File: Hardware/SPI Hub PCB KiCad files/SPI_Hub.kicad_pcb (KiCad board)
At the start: 4 copper layers, 90 x 65 mm, 22 parts, among them J1 Conn_01x08_Pin, J2 Left Front, J3 Left Center, J4 Left Rear, J5 Right Front, J6 Right Center, J7 Right Rear, U1 74AHC595, U2 74HC14

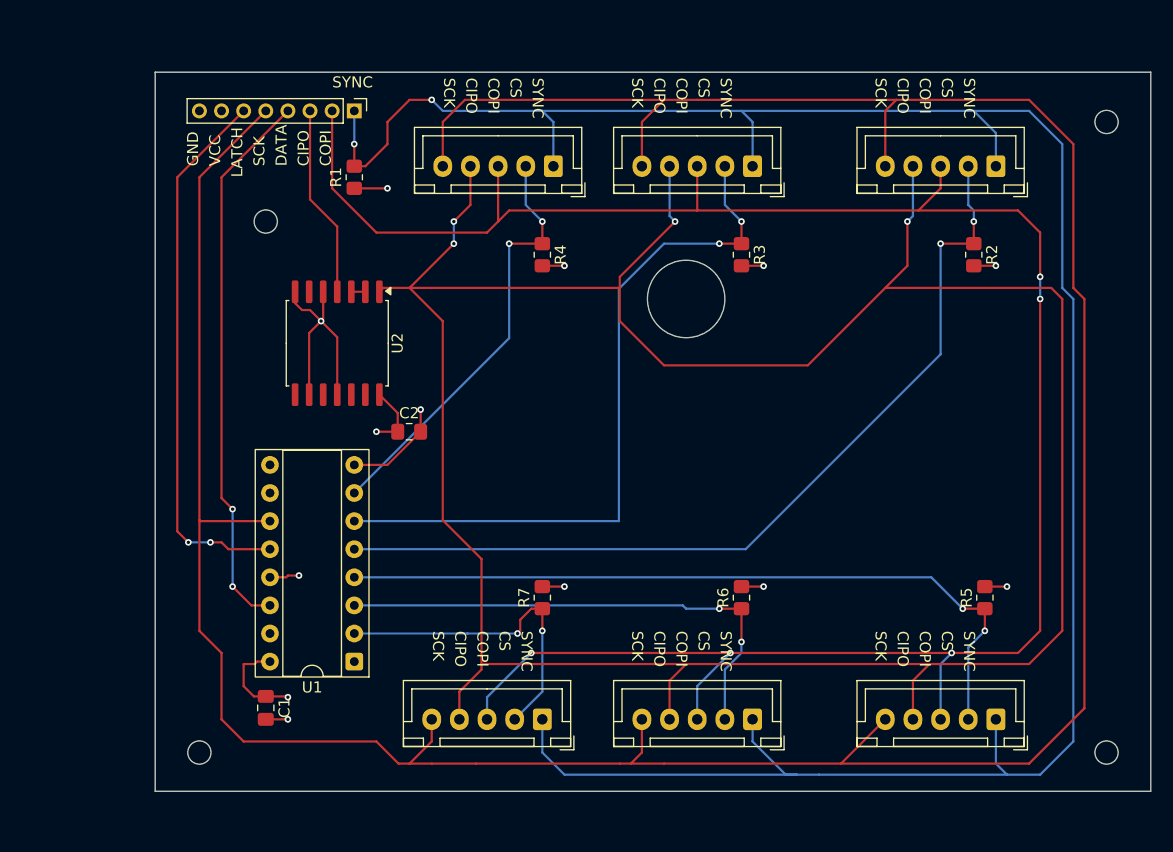
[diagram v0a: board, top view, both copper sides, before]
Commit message: Updated KiCad schematic, tied unused Schmitt input to gnd
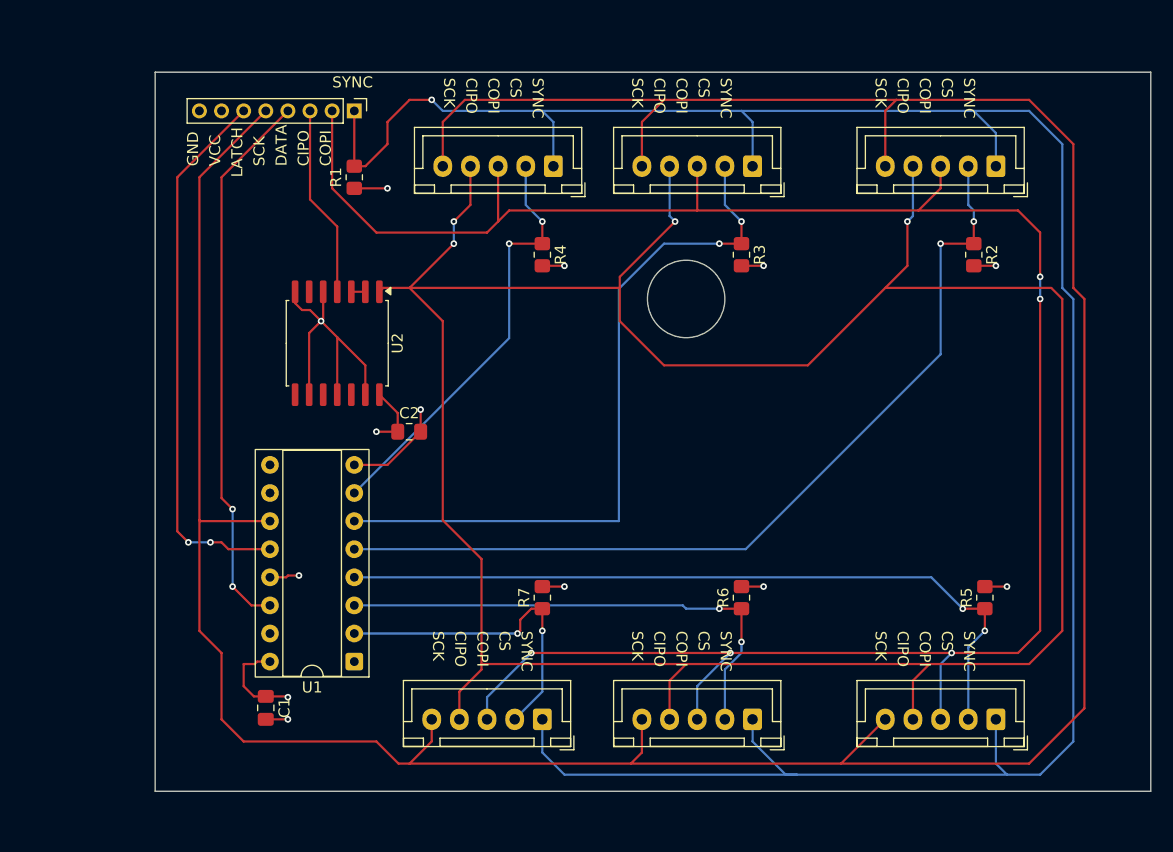
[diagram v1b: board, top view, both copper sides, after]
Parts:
- removed REF** (x4): MountingHole_2.1mm, MountingHole:MountingHole_2.1mm
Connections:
- net Net-(J2-Pin_4) renamed /cipo_peripheral
- U2 pad 13: unconnected-(U2-Pad13) -> GND
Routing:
- net GND: track 35.1 -> 41.3 mm
- net /trigger: track 211.8 -> 211.1 mm, vias 2 -> 1

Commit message: Updated and simplified PCB design
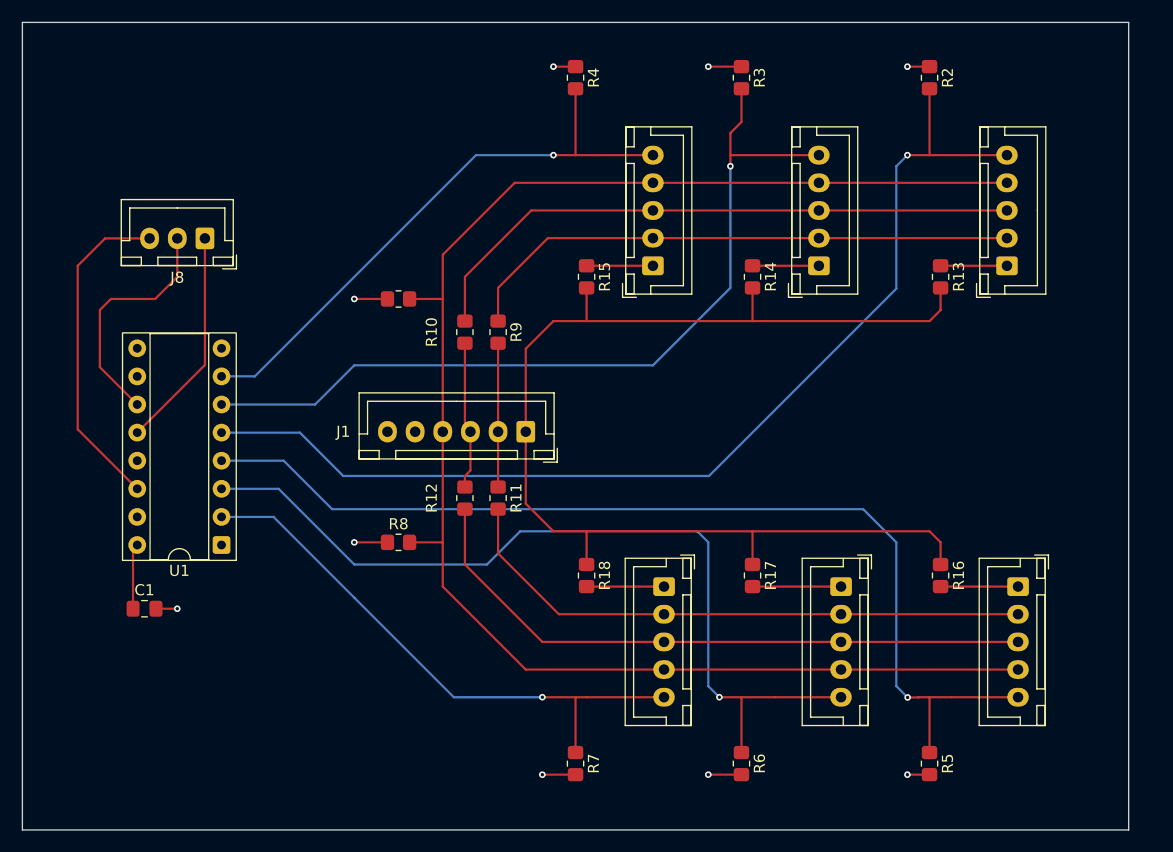
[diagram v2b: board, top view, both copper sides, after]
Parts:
- removed C2: 0.1 uF, Capacitor_SMD:C_0805_2012Metric_Pad1.18x1.45mm_HandSolder
- removed U2: 74HC14, Package_SO:SOIC-14W_7.5x9mm_P1.27mm
- added J8: Conn_01x03_Socket, Connector_JST:JST_XH_B3B-XH-A_1x03_P2.50mm_Vertical, F.Cu at (98.5, 72.5)
- added R10: 33, Resistor_SMD:R_0805_2012Metric_Pad1.20x1.40mm_HandSolder, F.Cu at (122.0, 81.0)
- added R11: 33, Resistor_SMD:R_0805_2012Metric_Pad1.20x1.40mm_HandSolder, F.Cu at (125.0, 96.0)
- added R12: 33, Resistor_SMD:R_0805_2012Metric_Pad1.20x1.40mm_HandSolder, F.Cu at (122.0, 96.0)
- added R13: R, Resistor_SMD:R_0805_2012Metric_Pad1.20x1.40mm_HandSolder, F.Cu at (165.0, 76.0)
- added R14: R, Resistor_SMD:R_0805_2012Metric_Pad1.20x1.40mm_HandSolder, F.Cu at (148.0, 76.0)
- added R15: R, Resistor_SMD:R_0805_2012Metric_Pad1.20x1.40mm_HandSolder, F.Cu at (133.0, 76.0)
- added R16: R, Resistor_SMD:R_0805_2012Metric_Pad1.20x1.40mm_HandSolder, F.Cu at (165.0, 103.0)
- added R17: R, Resistor_SMD:R_0805_2012Metric_Pad1.20x1.40mm_HandSolder, F.Cu at (148.0, 103.0)
- added R18: R, Resistor_SMD:R_0805_2012Metric_Pad1.20x1.40mm_HandSolder, F.Cu at (133.0, 103.0)
- added R8: 10k, Resistor_SMD:R_0805_2012Metric_Pad1.20x1.40mm_HandSolder, F.Cu at (116.0, 100.0)
- added R9: 33, Resistor_SMD:R_0805_2012Metric_Pad1.20x1.40mm_HandSolder, F.Cu at (125.0, 81.0)
- J1: value Conn_01x08_Pin -> Conn_01x06_Socket; footprint Connector_PinHeader_2.00mm:PinHeader_1x08_P2.00mm_Vertical -> Connector_JST:JST_XH_B6B-XH-A_1x06_P2.50mm_Vertical
- moved J1 32.9 mm to (127.5, 90.0), turned to 180 degrees
- moved R2 16.5 mm to (164.0, 58.0)
- moved J7 16.3 mm to (140.0, 104.0), turned to -90 degrees
- moved R4 16.3 mm to (132.0, 58.0)
- moved R3 16.0 mm to (147.0, 58.0)
- moved U1 16.0 mm to (100.0, 100.2)
- moved R5 15.8 mm to (164.0, 120.0), turned to -90 degrees
- moved R7 15.3 mm to (132.0, 120.0), turned to -90 degrees
- moved R6 15.0 mm to (147.0, 120.0), turned to -90 degrees
- moved J6 14.4 mm to (156.0, 104.0), turned to -90 degrees
- moved C1 14.2 mm to (93.0, 106.0), turned to 0 degrees
- moved J4 12.7 mm to (139.0, 75.0), turned to 90 degrees
- moved J5 12.2 mm to (172.0, 104.0), turned to -90 degrees
- moved R1 11.7 mm to (116.0, 78.0), turned to 0 degrees
- moved J3 10.8 mm to (154.0, 75.0), turned to 90 degrees
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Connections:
- J1 pad 1: /trigger -> /CIPO
- J1 pad 2: /copi -> Net-(J1-Pin_2)
- J1 pad 3: /cipo -> Net-(J1-Pin_3)
- J1 pad 4: /data -> /SYNC
- J1 pad 5: /sck -> +3.3V
- J1 pad 6: /latch -> GND
- J2 pad 1: /trigger -> Net-(J2-Pin_1)
- J2 pad 2: cs4 -> /COPI
- J2 pad 3: /copi -> /SCK
- J2 pad 4: /cipo_peripheral -> /SYNC
- J2 pad 5: /sck -> cs4
- J3 pad 1: /trigger -> Net-(J3-Pin_1)
- J3 pad 2: cs5 -> /COPI
- J3 pad 3: /copi -> /SCK
- J3 pad 4: /cipo_peripheral -> /SYNC
- J3 pad 5: /sck -> cs5
- J4 pad 1: /trigger -> Net-(J4-Pin_1)
- J4 pad 2: cs6 -> /COPI
- J4 pad 3: /copi -> /SCK
- J4 pad 4: /cipo_peripheral -> /SYNC
- J4 pad 5: /sck -> cs6
- J5 pad 1: /trigger -> Net-(J5-Pin_1)
- J5 pad 2: cs3 -> Net-(J5-Pin_2)
- J5 pad 3: /copi -> Net-(J5-Pin_3)
- J5 pad 4: /cipo_peripheral -> /SYNC
- J5 pad 5: /sck -> cs3
- J6 pad 1: /trigger -> Net-(J6-Pin_1)
- J6 pad 2: cs2 -> Net-(J5-Pin_2)
- J6 pad 3: /copi -> Net-(J5-Pin_3)
- J6 pad 4: /cipo_peripheral -> /SYNC
- J6 pad 5: /sck -> cs2
- J7 pad 1: /trigger -> Net-(J7-Pin_1)
- J7 pad 2: cs1 -> Net-(J5-Pin_2)
- J7 pad 3: /copi -> Net-(J5-Pin_3)
- J7 pad 4: /cipo_peripheral -> /SYNC
- J7 pad 5: /sck -> cs1
- R1 pad 2: /trigger -> /SYNC
- R2 pad 1: cs4 -> +3.3V
- R2 pad 2: +3.3V -> cs4
- R3 pad 1: cs5 -> +3.3V
- R3 pad 2: +3.3V -> cs5
- R4 pad 1: cs6 -> +3.3V
- R4 pad 2: +3.3V -> cs6
- U1 pad 11: /sck -> /SHCLK
- U1 pad 12: /latch -> /LATCH
- U1 pad 14: /data -> /DATA
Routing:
- net /sck: track 289.5 -> 0.00 mm
- net /cipo_peripheral: track 245.9 -> 0.00 mm, vias 4 -> 0
- net /trigger: track 211.1 -> 0.00 mm, vias 1 -> 0
- net /copi: track 192.3 -> 0.00 mm, vias 5 -> 0
- net /SYNC: track 0.00 -> 144.8 mm
- net /CIPO: track 0.00 -> 107.9 mm
- net Net-(J5-Pin_3): track 0.00 -> 57.9 mm
- net /SCK: track 0.00 -> 55.5 mm
- net Net-(J5-Pin_2): track 0.00 -> 53.3 mm
- net /COPI: track 0.00 -> 50.9 mm
- net /data: track 50.0 -> 0.00 mm, vias 2 -> 0
- net /latch: track 49.5 -> 0.00 mm, vias 2 -> 0
- net GND: track 41.3 -> 1.92 mm, vias 4 -> 1
- net cs2: track 45.7 -> 78.9 mm, vias 2 -> 1
- net /DATA: track 0.00 -> 29.9 mm
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- added copper zone on In1.Cu, net +3.3V
- added copper zone on In2.Cu, net GND
- removed copper zone on In2.Cu, net +3.3V
- removed copper zone on In1.Cu, net GND
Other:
- board size 90 x 65 mm -> 100 x 73 mm
- board text removed: "CIPO"
- board text removed: "COPI"
- board text removed: "CS"
- board text removed: "DATA"
- board text removed: "GND"
- board text removed: "LATCH"
- board text removed: "SCK"
- board text removed: "SYNC"
- board text removed: "VCC"
